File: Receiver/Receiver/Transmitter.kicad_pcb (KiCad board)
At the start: 4 copper layers, 40.3 x 98.2 mm, 71 parts, among them J1 SSW-104-01-T-D-LL, J10 Conn_01x03, J11 Conn_01x03, J12 Conn_01x03, J13 Conn_01x03, J14 Conn_01x03, J2 105-1103-001, J3 Conn_01x06, J4 105-1103-001, J5 105-1103-001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

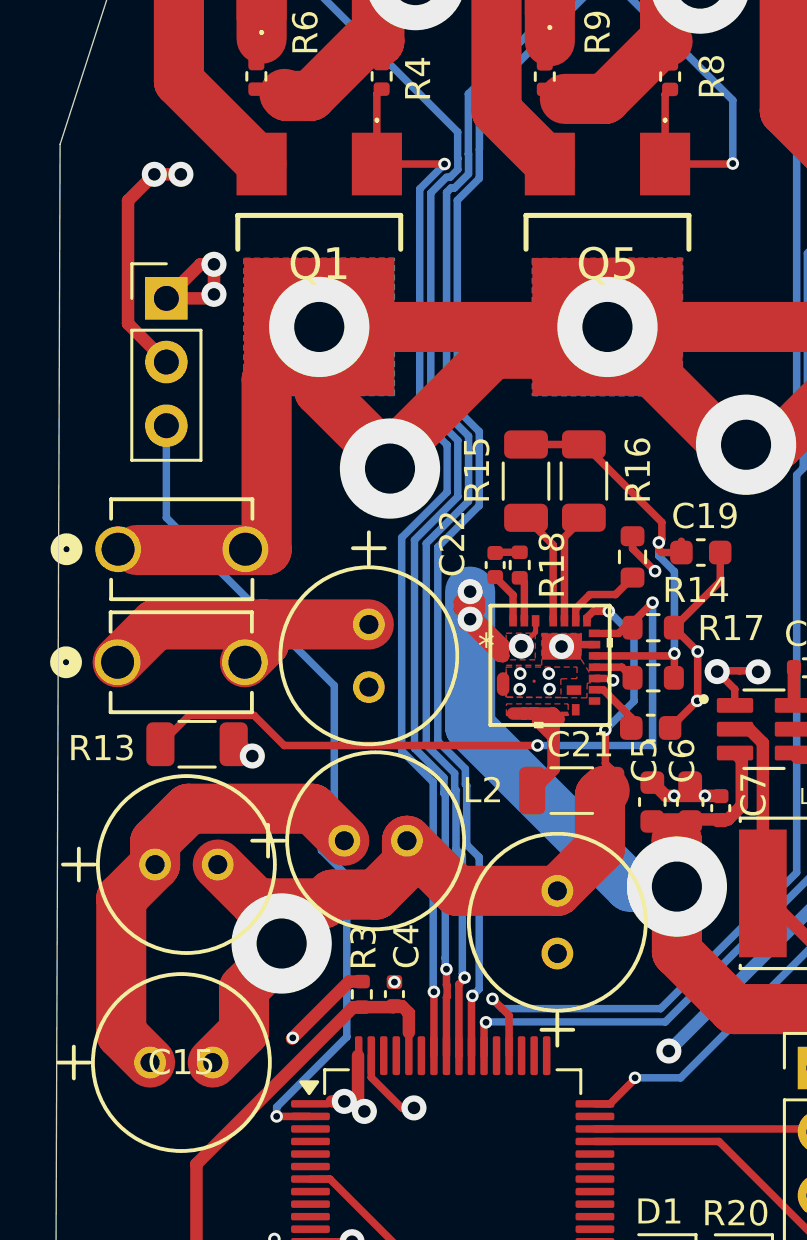
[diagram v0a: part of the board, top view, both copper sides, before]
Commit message: Updated KICAD files for V1, corrected SWDIO header
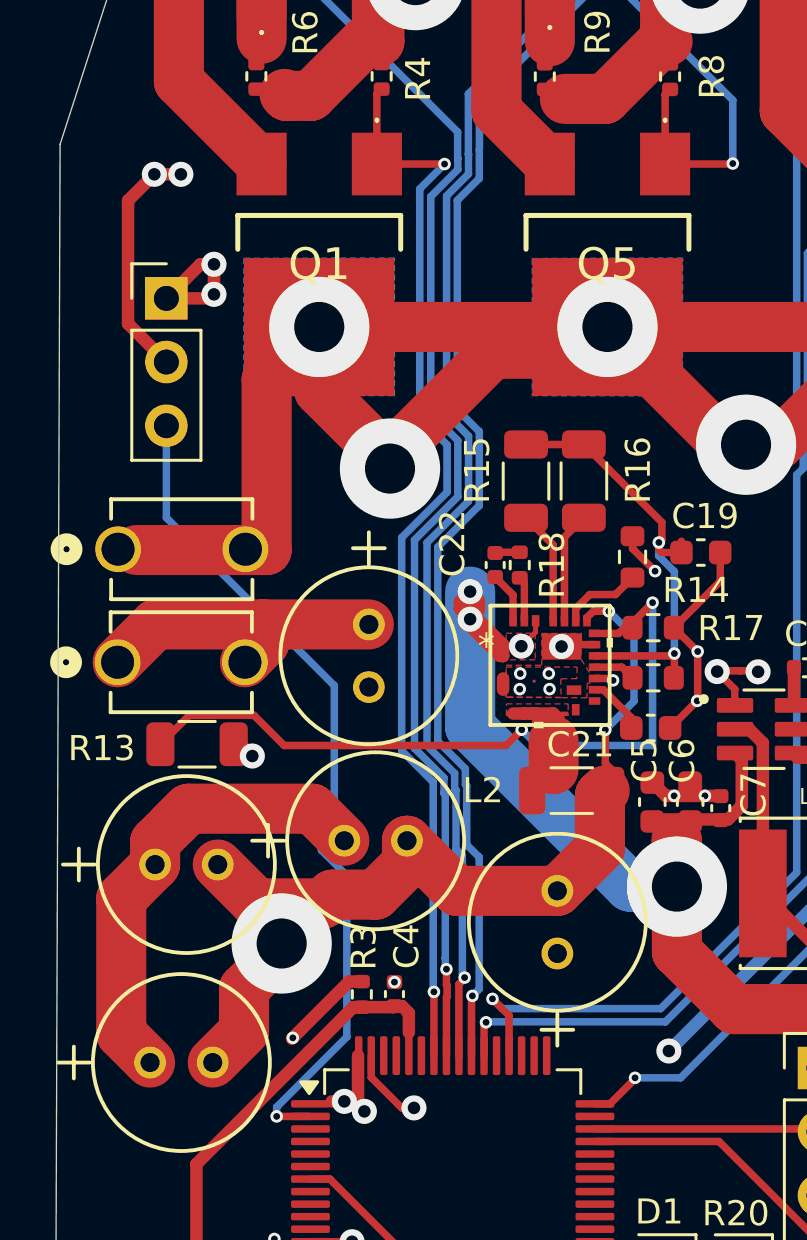
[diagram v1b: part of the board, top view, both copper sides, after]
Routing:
- net LBefore: track 6.59 -> 5.39 mm
- net Vfb: track 29.0 -> 29.5 mm

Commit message: PCB V2 updates
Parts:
- removed C3: 100nF, Capacitor_SMD:C_0402_1005Metric
- removed J6, J7: 105-1103-001, Libary1:CONN_105-1102-001
- added C23: 0.1uF, Capacitor_SMD:C_0402_1005Metric, F.Cu at (128.1, 107.8)
- added SW2: 500SSP1S2M2QEA, Libary1:500SSP1_EWI, F.Cu at (91.5, 62.8)
- added U7: HEF4104BT_653, Libary1:SO16_SOT109-1_NEX, B.Cu at (111.0, 50.4)
- C21: value 4.7uF -> 10uF
- C4: value 100nF -> 0.1uF
- J8, J9: value 105-1103-001 -> FCR7350R; footprint Libary1:CONN_105-1102-001 -> Libary1:CONN1_FCR7350R_CLF
- R2: value 4.7k -> 10k
- moved J8 54.2 mm to (121.9, 115.2)
- moved J9 49.9 mm to (97.6, 115.4)
- moved R2 21.3 mm to (113.2, 116.3)
- moved U1 18.2 mm to (127.6, 98.9)
- moved J12 17.5 mm to (89.4, 115.6), turned to 0 degrees
- moved J13 16.8 mm to (130.1, 115.1), turned to 0 degrees
- moved J1 11.0 mm to (109.8, 120.0)
- moved J14 9.73 mm to (106.3, 110.1), turned to 0 degrees
- moved R13 9.61 mm to (103.9, 71.0), turned to 90 degrees
- moved J10 6.08 mm to (90.2, 50.7)
- moved C17 5.92 mm to (92.2, 84.3)
- moved C15 5.62 mm to (92.2, 91.9)
- moved U3 5.15 mm to (125.6, 104.5), turned to 180 degrees
- moved C1 4.36 mm to (125.8, 108.3)
- moved C2 4.34 mm to (125.7, 106.9)
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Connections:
- J10 pad 1: +5V -> GND
- J10 pad 2: GND -> +5V
- J11 pad 1: +5V -> GND
- J11 pad 2: GND -> +5V
- J12 pad 1: +5V -> GND
- J12 pad 2: GND -> +5V
- J13 pad 1: +5V -> GND
- J13 pad 2: GND -> +5V
- J14 pad 1: +5V -> GND
- J14 pad 2: GND -> +5V
- J8 pad 1: Vbatt -> GND
- J8 pad 2: Vbatt -> (no net)
- J9 pad 1: Vdc -> Vbatt
- J9 pad 2: Vdc -> (no net)
- Q1 pad 1: S1 -> S1_BOOSTED
- Q5 pad 1: S3 -> S3_BOOSTED
- Q9 pad 1: S5 -> S5_BOOSTED
- R12 pad 1: S5 -> S5_BOOSTED
- R4 pad 1: S1 -> S1_BOOSTED
- R8 pad 1: S3 -> S3_BOOSTED
- U2 pad 41: unconnected-(U2-PA8-Pad41) -> DRIVER_ENABLE
- U2 pad 45: SWDIO -> unconnected-(U2-PA12-Pad45)
- U2 pad 46: SWCLK -> SWDIO
- U2 pad 49: unconnected-(U2-PA14-Pad49) -> SWCLK
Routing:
- net S5_BOOSTED: track 0.00 -> 27.8 mm, vias 0 -> 1
- net S3: track 63.6 -> 36.7 mm, vias 2 -> 3
- net Vbatt: track 105.6 -> 131.1 mm, vias 4 -> 5
- net +5V: track 85.5 -> 110.5 mm, vias 8 -> 6
- net Vdc: track 107.5 -> 127.3 mm, vias 9 -> 8
- net LElevator: track 16.5 -> 33.3 mm, vias 0 -> 1
- net RElevator: track 20.2 -> 35.7 mm
- net S1_BOOSTED: track 0.00 -> 15.1 mm, vias 0 -> 1
- net NRF_IRQ: track 29.8 -> 44.2 mm
- net GND: track 112.1 -> 98.4 mm, vias 27 -> 30
- net Vfb: track 29.5 -> 17.9 mm
- net S3_BOOSTED: track 0.00 -> 8.70 mm, vias 0 -> 1
- net SPI1_MISO: track 22.3 -> 29.5 mm
- net V_in: track 14.7 -> 21.2 mm
- net LFlap: track 33.5 -> 40.0 mm
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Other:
- board size 40.3 x 98.2 mm -> 44.6 x 98.5 mm

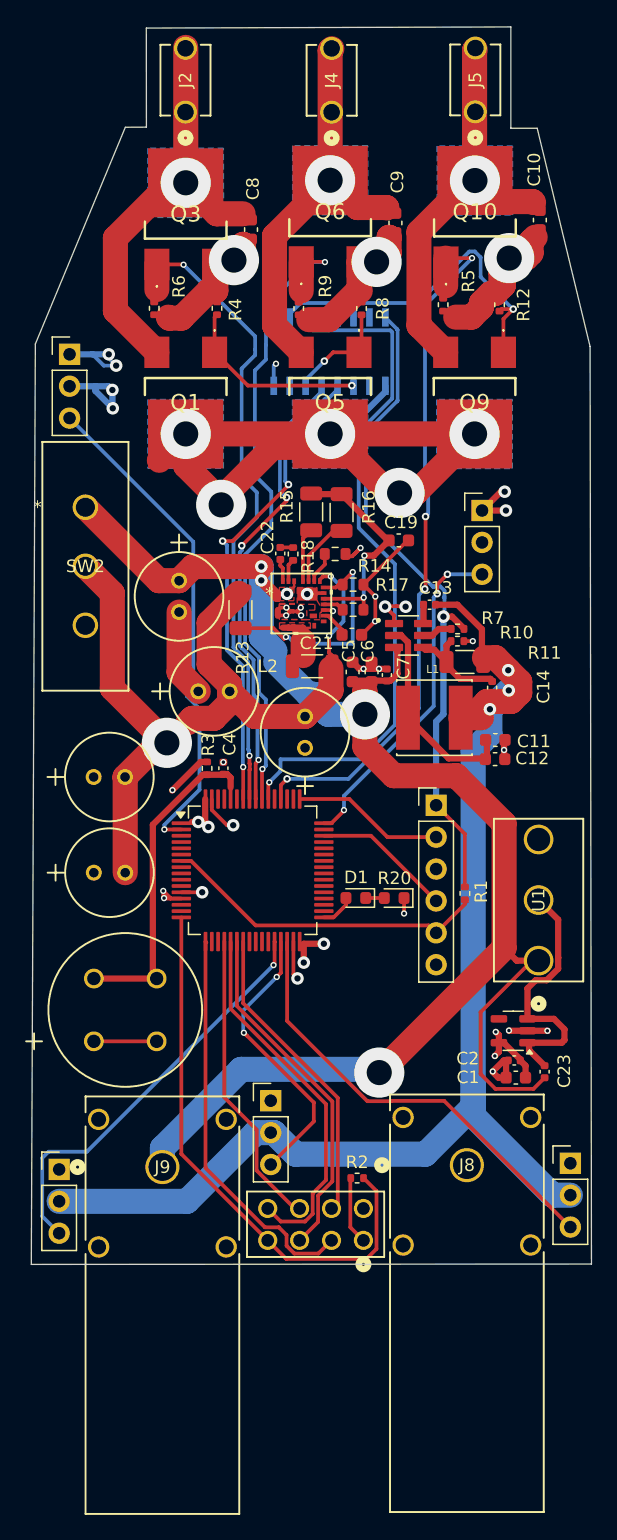
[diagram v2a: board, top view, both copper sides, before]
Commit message: Removed extra voltage converter and rerouted PCB
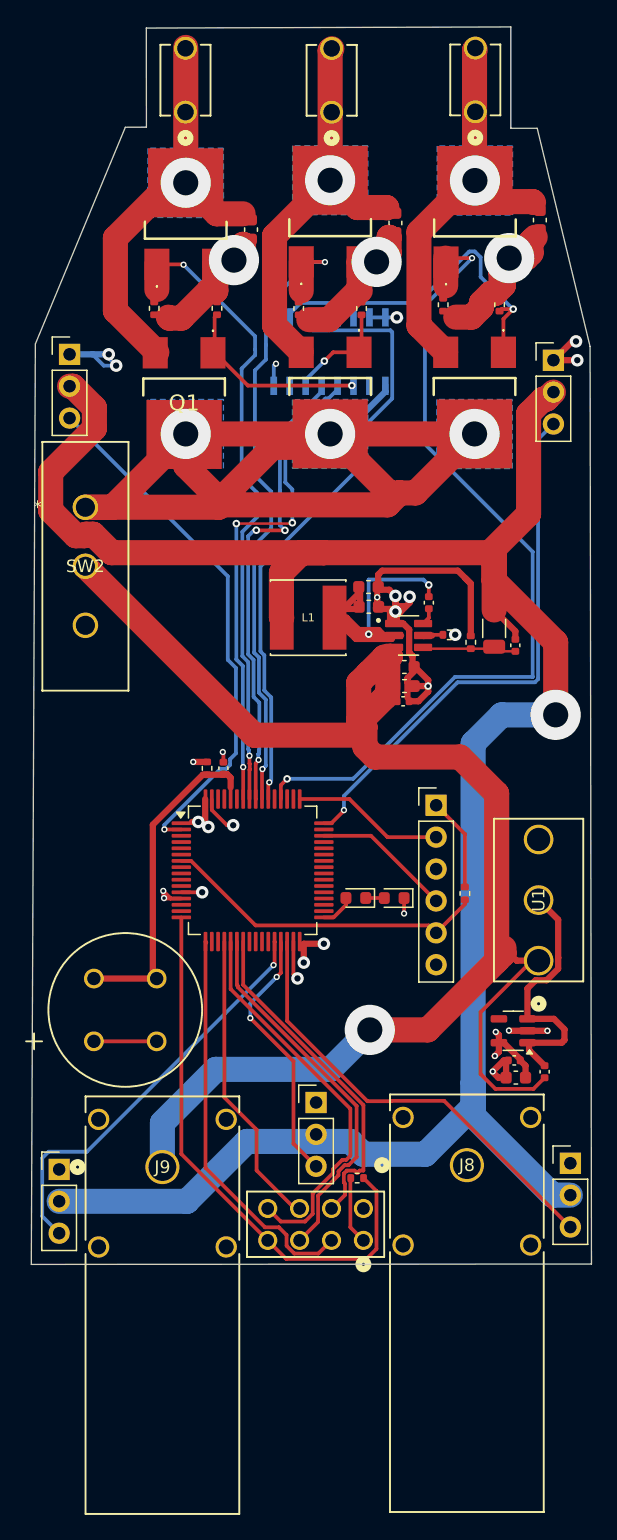
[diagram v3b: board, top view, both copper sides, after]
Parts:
- removed C15, C16, C17, C18, C20: 100uF, Libary1:100uFCap
- removed C19: 1uF, Capacitor_SMD:C_0603_1608Metric
- removed C21: 10uF, Capacitor_SMD:C_0603_1608Metric
- removed C22: 0.1uF, Capacitor_SMD:C_0402_1005Metric
- removed L2: 900nH, Inductor_SMD:L_1206_3216Metric
- removed R13: 180k, Resistor_SMD:R_1206_3216Metric
- removed R14, R17, R19: 10k, Resistor_SMD:R_0603_1608Metric
- removed R15: 100k, Resistor_SMD:R_1206_3216Metric
- removed R16: 51k, Resistor_SMD:R_1206_3216Metric
- removed R18: 1R, Resistor_SMD:R_0402_1005Metric
- removed U5: SIC431BED-T1-GE3, Libary1:QFN_ED-T1-GE3_VIS
- moved C11 15.8 mm to (114.1, 69.2)
- moved C12 15.8 mm to (114.1, 70.8)
- moved J11 13.2 mm to (128.8, 51.1)
- moved L1 12.8 mm to (109.2, 71.6), turned to 180 degrees
- moved C5 4.14 mm to (116.9, 75.6), turned to 0 degrees
- moved C14 3.84 mm to (125.8, 73.8), turned to -90 degrees
- moved J14 3.61 mm to (109.9, 110.2)
- moved R11 3.55 mm to (124.1, 72.5), turned to -90 degrees
- moved C6 2.85 mm to (116.9, 77.1), turned to 0 degrees
- moved C7 2.46 mm to (116.8, 78.3), turned to 0 degrees
- moved R10 1.06 mm to (122.2, 73.6), turned to -90 degrees
- moved R7 0.81 mm to (120.5, 73.0)
- moved C13 0.17 mm to (118.9, 70.4), turned to -90 degrees
- moved Q1 0.14 mm to (99.4, 55.3)
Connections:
- C13 pad 1: +5V -> Net-(U4-SW)
- SW2 pad 1: Vbatt -> Vdc
- SW2 pad 2: Vdc -> Vbatt
- U7 pad 15: DRIVER_ENABLE -> +3.3V
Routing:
- net +5V: track 110.5 -> 180.4 mm, vias 6 -> 1
- net +3.3V: track 79.6 -> 37.3 mm, vias 10 -> 11
- net Vdc: track 127.3 -> 95.3 mm, vias 8 -> 3
- net Vfb: track 17.9 -> 0.00 mm, vias 2 -> 0
- net Vdd: track 17.7 -> 0.00 mm, vias 2 -> 0
- net Net-(U4-SW): track 16.5 -> 33.8 mm, vias 0 -> 2
- net RFlap: track 27.3 -> 43.6 mm, vias 3 -> 1
- net S6: track 56.8 -> 67.5 mm, vias 4 -> 2
- net Vbatt: track 131.1 -> 124.3 mm, vias 5 -> 1
- net Net-(U5-MODE2): track 5.47 -> 0.00 mm
- net S5: track 55.1 -> 49.7 mm
- net GND: track 98.4 -> 103.6 mm, vias 30 -> 21
- net LBefore: track 4.53 -> 0.00 mm
- net Net-(U5-MODE1): track 4.32 -> 0.00 mm
- net NRF_CE: track 24.6 -> 27.3 mm
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- removed copper zone on In1.Cu, net +5V
- removed copper zone on F.Cu, net GND
- removed copper zone on F.Cu, net LBefore
- removed copper zone on F.Cu, net Vbatt
- removed copper zone on In1.Cu, net Vbatt
- removed copper zone on In1.Cu, net Vdc

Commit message: Added battery voltage sensing hardware to PCB
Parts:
- added R13: 300k, Resistor_SMD:R_0603_1608Metric, F.Cu at (96.5, 89.8)
- added R14: 100k, Resistor_SMD:R_0603_1608Metric, F.Cu at (96.5, 93.4)
- C8: value 10u -> 10uF
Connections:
- U2 pad 8: unconnected-(U2-PC0-Pad8) -> VBattSense
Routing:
- net Vdc: track 95.3 -> 122.1 mm, vias 3 -> 5
- net Net-(U2-BOOT0): track 26.2 -> 7.84 mm
- net VBattSense: track 0.00 -> 4.66 mm
- net GND: track 103.6 -> 104.8 mm, vias 21 -> 22
- net Vbatt: track 124.3 -> 125.0 mm

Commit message: V2 PCB
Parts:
- added C15: 1uF, Capacitor_SMD:C_0402_1005Metric, F.Cu at (100.2, 79.3)
- added C16: 0.1uF, Capacitor_SMD:C_0402_1005Metric, F.Cu at (107.0, 78.3)
- added C17: 0.1uF, Capacitor_SMD:C_0402_1005Metric, F.Cu at (90.9, 89.5)
- added C18: 1uF, Capacitor_SMD:C_0402_1005Metric, F.Cu at (92.4, 92.0)
- added C3: 1uF, Capacitor_SMD:C_0402_1005Metric, F.Cu at (105.2, 79.5)
- added R15: 10k, Resistor_SMD:R_0402_1005Metric, F.Cu at (102.1, 77.3)
- added R16: 10k, Resistor_SMD:R_0402_1005Metric, F.Cu at (102.1, 78.2)
- added U5: ICM-20948, Sensor_Motion:InvenSense_QFN-24_3x3mm_P0.4mm, F.Cu at (109.7, 77.5)
- added U8: MIC5365-1.8YC5-TR, Libary1:SC-70_C5_MCH, F.Cu at (92.7, 89.4)
- moved SW2 7.79 mm to (95.3, 69.6)
- moved R14 1.54 mm to (94.9, 93.5)
- moved R13 1.54 mm to (95.0, 89.8)
- moved C10 1.51 mm to (126.3, 39.5)
- moved C8 1.51 mm to (103.3, 40.2)
- moved C9 1.51 mm to (114.8, 39.7)
- moved J2 1.51 mm to (98.1, 30.9)
- moved J5 1.51 mm to (121.1, 30.8)
- moved Q1 1.51 mm to (97.9, 54.8)
- moved Q10 1.51 mm to (121.1, 38.0)
- moved J4 1.51 mm to (109.7, 30.9)
- moved Q3 1.51 mm to (98.1, 38.2)
- moved Q6 1.51 mm to (109.6, 38.0)
- moved R12 1.51 mm to (123.1, 46.2)
- moved R4 1.51 mm to (100.6, 46.5)
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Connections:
- U2 pad 4: unconnected-(U2-PC15-Pad4) -> INT_sense
- U2 pad 5: unconnected-(U2-PF0-Pad5) -> IC21_SDA
- U2 pad 6: unconnected-(U2-PF1-Pad6) -> IC21_SCL
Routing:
- net IC21_SCL: track 0.00 -> 43.5 mm
- net IC21_SDA: track 0.00 -> 41.1 mm
- net Vddio_sensor: track 0.00 -> 28.7 mm, vias 0 -> 2
- net INT_sense: track 0.00 -> 21.4 mm, vias 0 -> 2
- net Net-(U2-BOOT0): track 7.84 -> 29.2 mm, vias 0 -> 2
- net GND: track 104.8 -> 122.5 mm, vias 22 -> 28
- net +3.3V: track 37.3 -> 47.0 mm, vias 11 -> 16
- net +5V: track 180.4 -> 174.7 mm, vias 1 -> 2
- net Vbatt: track 125.0 -> 119.4 mm
- net VBattSense: track 4.66 -> 6.04 mm
- net LFlap: track 42.2 -> 43.5 mm
- net Net-(U5-REGOUT): track 0.00 -> 1.14 mm
- net S6: track 67.5 -> 68.6 mm
- net S1: track 39.7 -> 40.8 mm
- net S4: track 51.6 -> 52.7 mm
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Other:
- board size 44.6 x 98.5 mm -> 44.1 x 98.6 mm
